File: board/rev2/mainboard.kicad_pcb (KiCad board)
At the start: 2 copper layers, 155 parts, among them Q1 WSD40120DN56G, SW1 MS-22D28-G020, SW2 MS-22D28-G020, SW3 MS-22D28-G020, SW4 TS-1088-AR02016, SW5 MS-22D28-G020, U1 TPD6S300A, U10 74VHC161, U11 IS61LV256AL, U12 74AHCT595, U13 IS61LV256AL, U14 74AHCT595, U15 74HCT245, U16 74HCT245, U17 TS3USB30ERSWR, U18 TS3USB30ERSWR, U2 TPS62933, U3 TPS259472A, U4 LM5050-1, U5 SiC451, U6 STM32G071CBUx, U7 ESP32-C6-WROOM-1, U8 TLV74311, U9 RP2354B, Y1 ABM8-272-T3

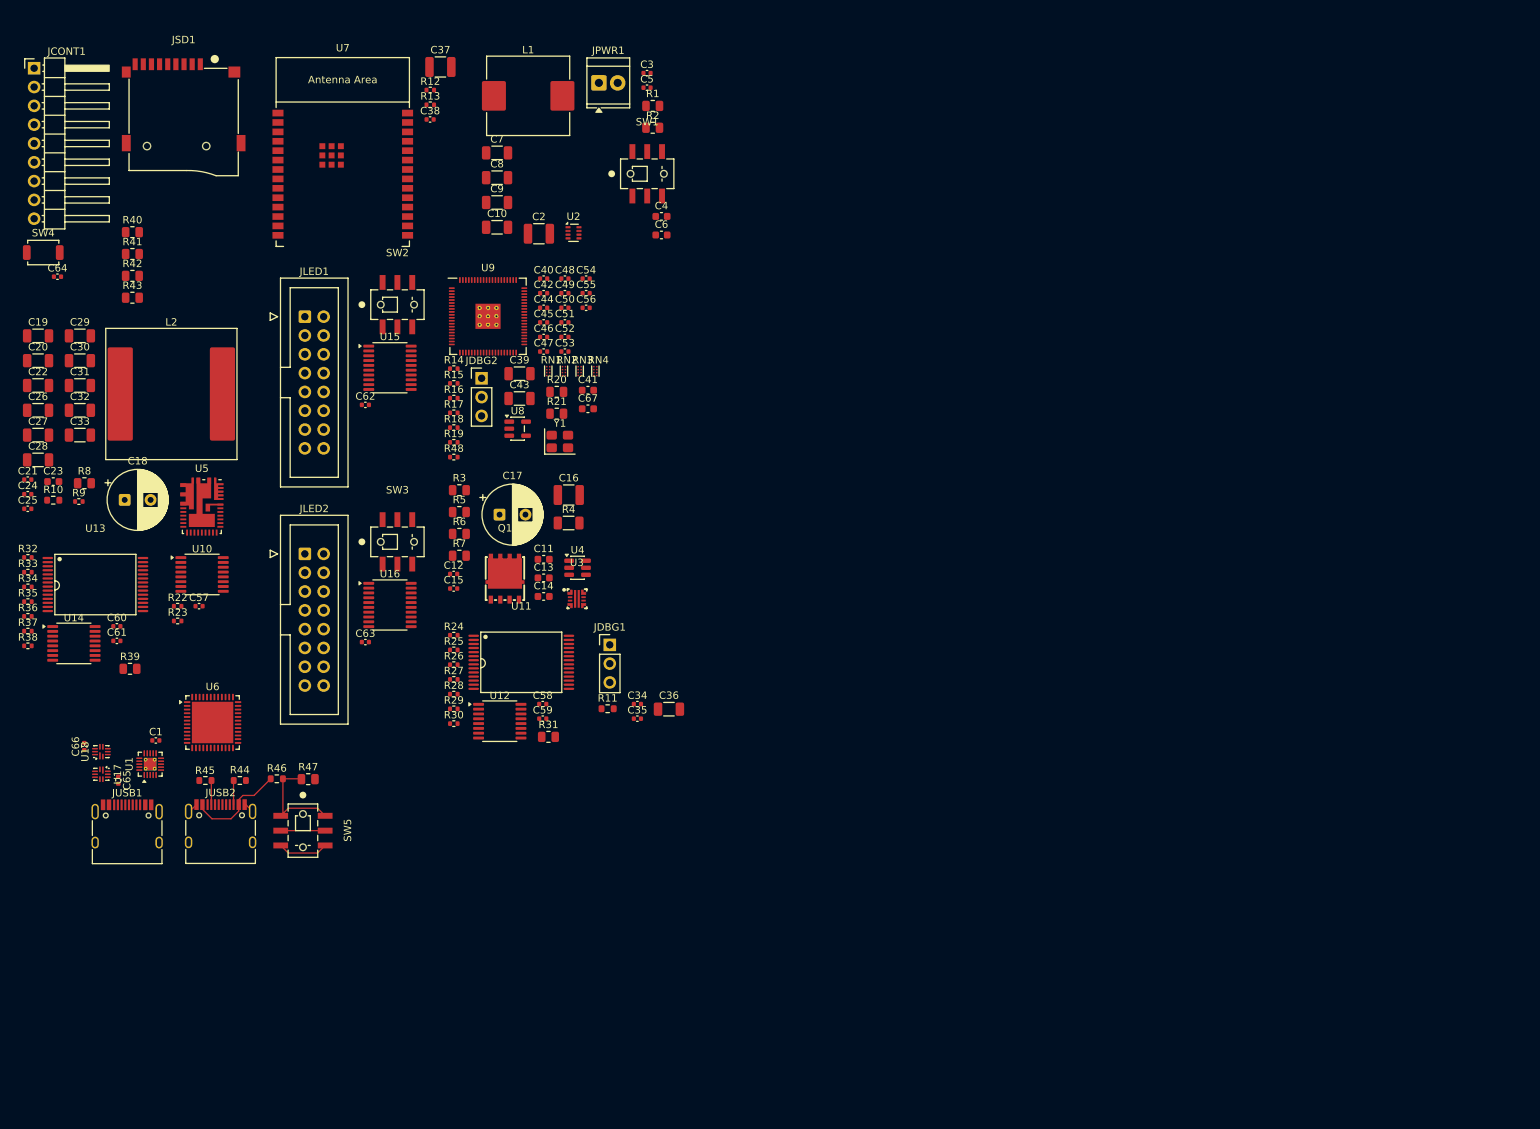
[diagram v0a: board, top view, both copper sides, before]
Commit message: More tweaks to schematic, start laying out regulators
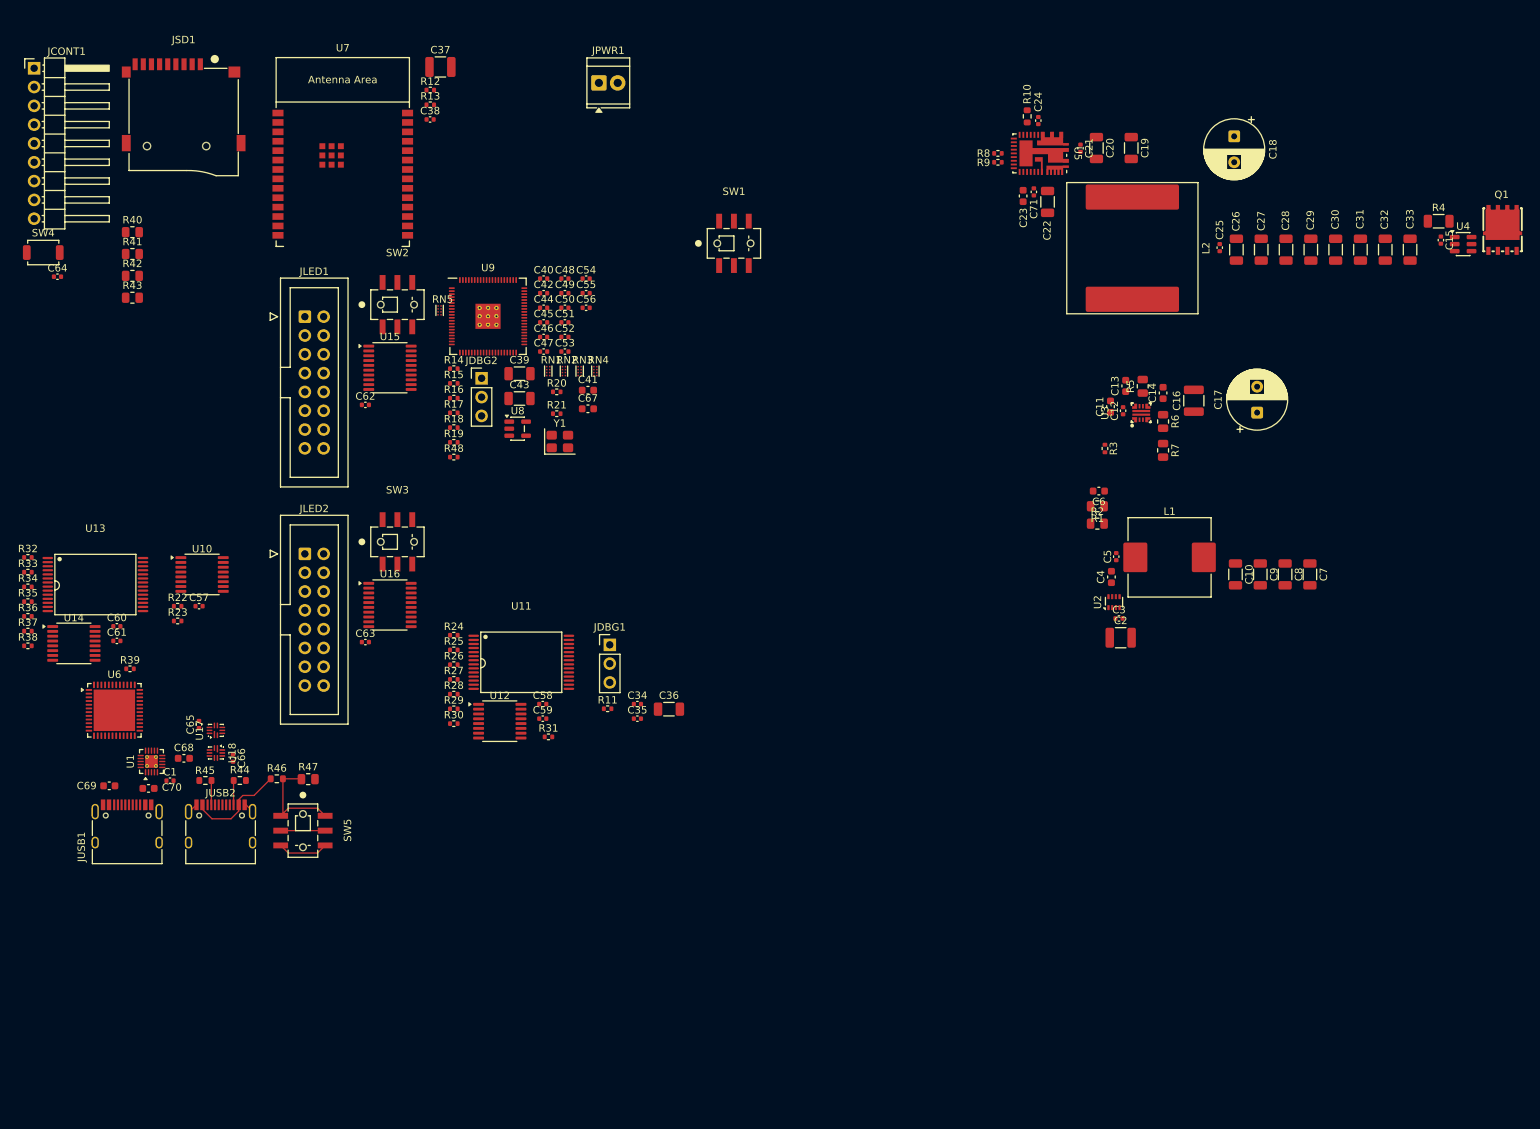
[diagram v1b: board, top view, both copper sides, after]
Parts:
- added C68: 1uF, Capacitor_SMD:C_0603_1608Metric, F.Cu at (67.6, 122.8)
- added C69: 330pF, Capacitor_SMD:C_0603_1608Metric, F.Cu at (57.5, 126.5)
- added C70: 330pF, Capacitor_SMD:C_0603_1608Metric, F.Cu at (62.9, 126.9)
- added C71: 100nF, Capacitor_SMD:C_0402_1005Metric, F.Cu at (182.4, 46.4)
- added RN5: 33, RN_SMD:R_Array_Flat_4x0201, F.Cu at (102.2, 62.4)
- R11: footprint Resistor_SMD:R_0603_1608Metric -> Resistor_SMD:R_0402_1005Metric
- R20, R21, R3, R31, R39, R8: footprint Resistor_SMD:R_0805_2012Metric -> Resistor_SMD:R_0402_1005Metric
- moved C33 181.4 mm to (233.2, 54.1), turned to 90 degrees
- moved C32 177.6 mm to (229.8, 54.1), turned to 90 degrees
- moved C31 173.9 mm to (226.5, 54.1), turned to 90 degrees
- moved C28 170.9 mm to (216.4, 54.1), turned to 90 degrees
- moved C30 170.2 mm to (223.2, 54.1), turned to 90 degrees
- moved C27 167.1 mm to (213.1, 54.1), turned to 90 degrees
- moved C29 166.6 mm to (219.8, 54.1), turned to 90 degrees
- moved C25 164.8 mm to (207.5, 53.9), turned to 90 degrees
- moved C26 163.3 mm to (209.8, 54.1), turned to 90 degrees
- moved C18 157.7 mm to (209.4, 38.8), turned to -90 degrees
- moved C19 149.8 mm to (195.6, 40.4), turned to -90 degrees
- moved C21 149.0 mm to (188.7, 40.5), turned to -90 degrees
- moved C20 145.8 mm to (190.8, 40.4), turned to -90 degrees
- moved C24 145.5 mm to (183.0, 36.7), turned to 90 degrees
- moved Q1 142.7 mm to (245.7, 51.5)
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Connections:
- C10 pad 2: Net-(C10-Pad2) -> GND
- C2 pad 2: Net-(C10-Pad2) -> GND
- C3 pad 2: Net-(C10-Pad2) -> GND
- C4 pad 2: Net-(C10-Pad2) -> GND
- C7 pad 2: Net-(C10-Pad2) -> GND
- C8 pad 2: Net-(C10-Pad2) -> GND
- C9 pad 2: Net-(C10-Pad2) -> GND
- R2 pad 2: Net-(C10-Pad2) -> GND
- U1 pad 19: /Peripherals/AUX_USB_D- -> GND
- U1 pad 20: /Peripherals/AUX_USB_D+ -> GND
- U18 pad 1: /Peripherals/AUX_USB_D+ -> /Peripherals/AUX_USB_D-
- U18 pad 2: /Power/USB_D+ -> /Power/USB_D-
- U18 pad 3: /USB Mux/ESP_D+ -> /USB Mux/ESP_D-
- U18 pad 5: /USB Mux/ESP_D- -> /USB Mux/ESP_D+
- U18 pad 6: /Power/USB_D- -> /Power/USB_D+
- U18 pad 7: /Peripherals/AUX_USB_D- -> /Peripherals/AUX_USB_D+
- U9 pad 11: /Decoder/Output Stage A/PIX_RGB_Q1 -> /Display MCU/ESP_INT
- U9 pad 8: /Display MCU/ESP_INT -> Net-(RN5-R1.1)
- U9 pad 9: /Decoder/Output Stage A/PIX_RGB_Q0 -> Net-(RN5-R3.1)
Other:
- copper layers 2 -> 4

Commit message: 3.3V LDO
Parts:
- removed RN1, RN2, RN3, RN4, RN5: 33, RN_SMD:R_Array_Flat_4x0201
- added C72: 10uF, Capacitor_SMD:C_1210_3225Metric, F.Cu at (238.6, 96.7)
- added C73: 47uF, Capacitor_SMD:C_1206_3216Metric, F.Cu at (224.0, 95.2)
- added R49: 33, Resistor_SMD:R_0402_1005Metric, F.Cu at (101.5, 63.6)
- added R50: 33, Resistor_SMD:R_0402_1005Metric, F.Cu at (101.5, 65.6)
- added R51: 33, Resistor_SMD:R_0402_1005Metric, F.Cu at (101.5, 67.6)
- added U19: LD1117AG-33-AA3-A-R, Package_TO_SOT_SMD:SOT-223-3_TabPin2, F.Cu at (231.8, 95.4)
- C10: value 47uF -> 10uF; footprint Capacitor_SMD:C_1206_3216Metric -> Capacitor_SMD:C_1210_3225Metric
- C6: value 22pF -> 10pF; footprint Capacitor_SMD:C_0603_1608Metric -> Capacitor_SMD:C_0402_1005Metric
- L1: value 4.7uH -> 6.8uH; footprint Inductor_SMD:L_TechFuse_SL1040 -> Inductor_SMD:L_Chilisin_BMRF00101040
- R1: value 47k -> 49.9k; footprint Resistor_SMD:R_0805_2012Metric -> Resistor_SMD:R_0603_1608Metric
- R2: value 15k -> 10k; footprint Resistor_SMD:R_0805_2012Metric -> Resistor_SMD:R_0402_1005Metric
- moved R23 55.0 mm to (101.5, 61.6)
- moved R22 55.0 mm to (101.5, 59.6)
- moved C10 30.3 mm to (239.3, 92.3), turned to 0 degrees
- moved R16 16.7 mm to (101.5, 57.7)
- moved C4 5.72 mm to (194.2, 92.8)
- moved U2 5.60 mm to (194.3, 96.2)
- moved C2 5.54 mm to (195.1, 101.1)
- moved C3 5.54 mm to (194.9, 98.5)
- moved R1 5.28 mm to (191.6, 94.0), turned to 0 degrees
- moved C6 4.63 mm to (192.1, 91.3), turned to 0 degrees
- moved L1 4.25 mm to (204.1, 93.0)
- moved C5 3.77 mm to (196.2, 93.0)
- moved C8 2.90 mm to (216.8, 95.2)
- moved C9 2.90 mm to (213.5, 95.2)
- moved C7 2.90 mm to (220.2, 95.2)
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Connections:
- C10 pad 1: VDD -> Net-(U19-VI)
- C6 pad 1: VDD -> Net-(U19-VI)
- C7 pad 1: VDD -> Net-(U19-VI)
- C8 pad 1: VDD -> Net-(U19-VI)
- C9 pad 1: VDD -> Net-(U19-VI)
- L1 pad 2: VDD -> Net-(U19-VI)
- R1 pad 1: VDD -> Net-(U19-VI)
- R16 pad 1: Net-(U9-GPIO20) -> Net-(U9-GPIO10)
- R16 pad 2: /Decoder/PIX_MEM_PA4 -> /Decoder/Output Stage A/PIX_RGB_Q0
- R22 pad 1: /Decoder/RGB_CLK -> Net-(U9-GPIO10)
- R22 pad 2: /Decoder/Output Stage A/RGB_CLK -> /Decoder/Output Stage A/PIX_RGB_Q0
- R23 pad 1: /Decoder/RGB_CLK -> Net-(U9-GPIO11)
- R23 pad 2: /Decoder/Output Stage B/RGB_CLK -> /Decoder/Output Stage A/PIX_RGB_Q1
- U12 pad 11: /Decoder/Output Stage A/RGB_CLK -> /Decoder/RGB_CLK
- U14 pad 11: /Decoder/Output Stage B/RGB_CLK -> /Decoder/RGB_CLK
- U9 pad 11: /Display MCU/ESP_INT -> Net-(U9-GPIO12)
- U9 pad 12: /Decoder/RGB_CLK -> /Display MCU/ESP_INT
- U9 pad 16: Net-(RN1-R1.1) -> /Decoder/PIX_MEM_PA0
- U9 pad 17: Net-(RN1-R2.1) -> /Decoder/PIX_MEM_PA1
- U9 pad 18: Net-(RN1-R3.1) -> /Decoder/PIX_MEM_PA2
- U9 pad 19: Net-(RN1-R4.1) -> /Decoder/PIX_MEM_PA3
- U9 pad 20: Net-(U9-GPIO20) -> /Decoder/PIX_MEM_PA4
- U9 pad 21: Net-(RN2A-R1.1) -> /Decoder/PIX_MEM_PA5
- U9 pad 22: Net-(RN2B-R2.1) -> /Decoder/PIX_MEM_PA6
- U9 pad 23: Net-(RN2C-R3.1) -> /Decoder/PIX_MEM_PA7
- U9 pad 25: Net-(RN3-R1.1) -> /Decoder/PIX_MEM_PB0
- U9 pad 26: Net-(RN3-R2.1) -> /Decoder/PIX_MEM_PB1
- U9 pad 27: Net-(RN3-R3.1) -> /Decoder/PIX_MEM_PB2
- U9 pad 28: Net-(RN3-R4.1) -> /Decoder/PIX_MEM_PB3
- U9 pad 36: Net-(RN4-R1.1) -> /Decoder/PIX_MEM_PB4
- U9 pad 37: Net-(RN4-R2.1) -> /Decoder/PIX_MEM_PB5
- U9 pad 38: Net-(RN4-R3.1) -> /Decoder/PIX_MEM_PB6
- U9 pad 39: Net-(RN4-R4.1) -> /Decoder/PIX_MEM_PB7
- U9 pad 8: Net-(RN5-R1.1) -> Net-(U9-GPIO10)
- U9 pad 9: Net-(RN5-R3.1) -> Net-(U9-GPIO11)

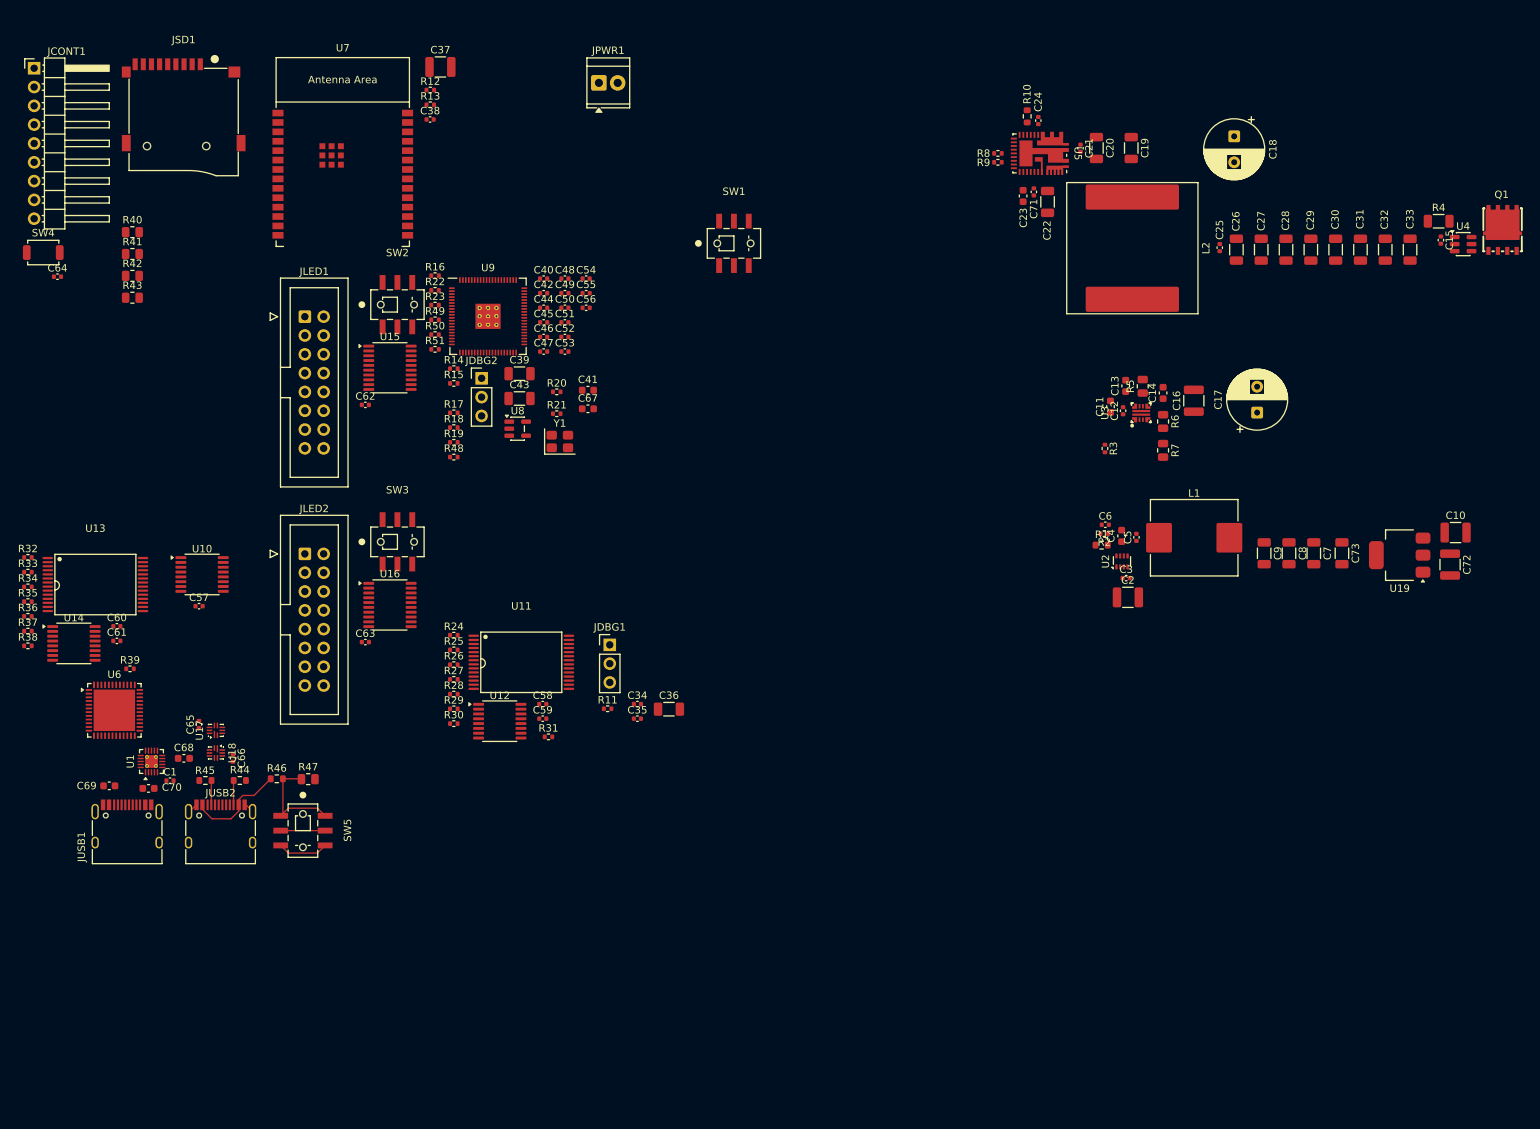
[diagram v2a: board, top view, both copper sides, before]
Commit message: Layout more component blocks
- regulators
- mcus

Still need to do the decoders + overall packing
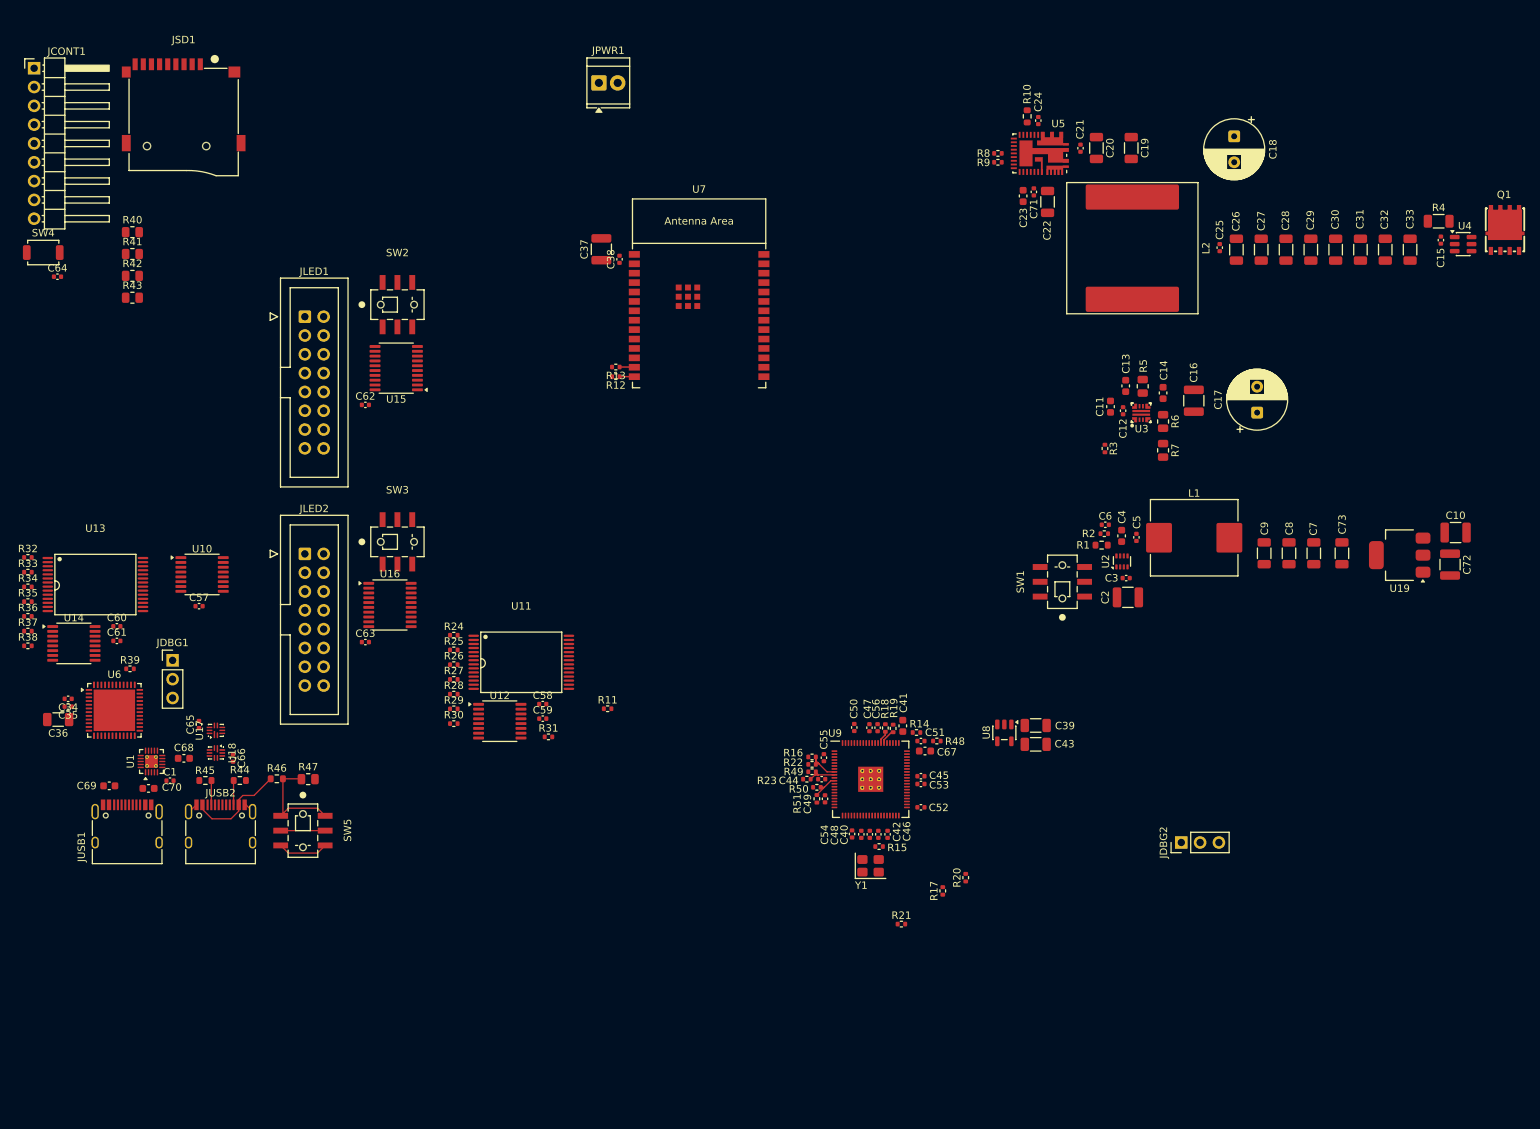
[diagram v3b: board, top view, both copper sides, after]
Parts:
- moved JDBG2 113.4 mm to (202.3, 134.2), turned to 90 degrees
- moved R17 92.3 mm to (170.1, 140.7), turned to 90 degrees
- moved C40 87.0 mm to (160.2, 133.1), turned to 90 degrees
- moved C42 85.9 mm to (161.4, 133.1), turned to -90 degrees
- moved R20 85.8 mm to (173.2, 138.9), turned to 90 degrees
- moved C48 85.0 mm to (159.1, 133.1), turned to 90 degrees
- moved R15 84.9 mm to (161.5, 134.8), turned to 180 degrees
- moved C39 84.4 mm to (182.7, 118.4)
- moved C43 83.9 mm to (182.7, 121.0)
- moved R21 83.2 mm to (164.5, 145.2)
- moved C54 83.1 mm to (157.8, 133.1), turned to 90 degrees
- moved R16 82.6 mm to (152.4, 122.7), turned to 180 degrees
- moved C36 82.5 mm to (50.6, 117.6), turned to 180 degrees
- moved R22 81.8 mm to (152.4, 123.7), turned to 180 degrees
- moved C46 81.7 mm to (162.7, 133.1), turned to 90 degrees
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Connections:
- U9 pad 12: /Display MCU/ESP_INT -> /Display MCU/~{PIX_CLK}
- U9 pad 13: /Display MCU/~{PIX_CLK} -> /Decoder/PIX_CLK
- U9 pad 14: /Decoder/PIX_CLK -> /Display MCU/ESP_INT
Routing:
- net Net-(U9-GPIO10): track 0.00 -> 5.26 mm
- net Net-(U9-GPIO11): track 0.00 -> 4.97 mm
- net Net-(U9-GPIO12): track 0.00 -> 4.16 mm
- net /Display MCU/MCU_USB_D-: track 0.00 -> 2.09 mm
- net /WiFi MCU/MCU_USB_D-: track 0.00 -> 2.00 mm
- net /WiFi MCU/MCU_USB_D+: track 0.00 -> 1.99 mm
- net /Display MCU/MCU_USB_D+: track 0.00 -> 1.76 mm
